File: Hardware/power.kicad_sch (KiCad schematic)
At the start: 57 parts, among them J8 DeployLipo, J9 UCLipo, Q10 DMP3099L, Q6 SI4143DY-T1-GE3, Q7 SI4143DY-T1-GE3, Q8 DMP3099L, Q9 DMP3099L, U10 LTC4412xS6, U11 MP28167GQ-A-Z, U14 LTC4412xS6, U16 SC4215, U17 LTC4412xS6, U22 LTC4412xS6, U9 LTC4412xS6

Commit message: black edition ordering stuff
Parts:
- added C37: 0.1uF, Capacitor_SMD:C_0402_1005Metric, symbol Device:C_Small
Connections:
- net GND: now also C37.1
- net UC_Lipo_Scaled: now also C37.2
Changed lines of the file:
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@@
   (junction (at 204.47 85.09) (diameter 0) (color 0 0 0 0)
   )
+  (junction (at 96.52 45.72) (diameter 0) (color 0 0 0 0)
+  )
   (junction (at 271.78 38.1) (diameter 0) (color 0 0 0 0)
   )
@@
   )
   (junction (at 38.1 160.02) (diameter 0) (color 0 0 0 0)
+  )
+  (junction (at 87.63 52.07) (diameter 0) (color 0 0 0 0)
   )
   (junction (at 207.01 90.17) (diameter 0) (color 0 0 0 0)
@@
   (no_connect (at 219.71 50.8))
   (no_connect (at 67.31 129.54))
-  (wire (pts (xy 87.63 45.72) (xy 100.33 45.72))
+  (wire (pts (xy 87.63 45.72) (xy 96.52 45.72))
     (stroke (width 0) (type default))
   )
@@
     (stroke (width 0) (type default))
   )
+  (wire (pts (xy 87.63 52.07) (xy 96.52 52.07))
+    (stroke (width 0) (type default))
+  )
   (wire (pts (xy 109.22 72.39) (xy 102.87 72.39))
     (stroke (width 0) (type default))
@@
     (stroke (width 0) (type default))
   )
+  (wire (pts (xy 96.52 46.99) (xy 96.52 45.72))
+    (stroke (width 0) (type default))
+  )
   (wire (pts (xy 271.78 83.82) (xy 281.94 83.82))
     (stroke (width 0) (type default))
@@
   )
   (wire (pts (xy 251.46 144.78) (xy 257.81 144.78))
+    (stroke (width 0) (type default))
+  )
+  (wire (pts (xy 96.52 45.72) (xy 100.33 45.72))
     (stroke (width 0) (type default))
   )
@@
         )
       )
+    )
+  )
+  (symbol (lib_id "Device:C_Small") (at 96.52 49.53 180) (unit 1)
+    (in_bom yes) (on_board yes) (dnp no)
+    (property "Reference" "C37" (at 99.4783 48.8354 0)
+      (effects (font (size 1.27 1.27)) (justify right) hide)
+    )
+    (property "Value" "0.1uF" (at 99.4783 51.3754 0)
+      (effects (font (size 1.27 1.27)) (justify right) hide)
+    )
+    (property "Footprint" "Capacitor_SMD:C_0402_1005Metric" (at 96.52 49.53 0)
+      (effects (font (size 1.27 1.27)) hide)
+    )
+    (property "Datasheet" "~" (at 96.52 49.53 0)
+      (effects (font (size 1.27 1.27)) hide)
+    )
+    (pin "1")
+    (pin "2")
+    (instances
+      (project "PickleRick"
+        (path "/e63e39d7-6ac0-4ffd-8aa3-1841a4541b55/150d7a0e-7d8c-4788-bc30-4a3682bf4d09"
+          (reference "C37") (unit 1)
+        )
+      )

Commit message: v3 hardware start
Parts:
- removed Q6, Q7: SI4143DY-T1-GE3, Package_SO:SOIC-8_3.9x4.9mm_P1.27mm, symbol Device:Q_PMOS_GDS
- added C58: 0.1uF, Capacitor_SMD:C_0402_1005Metric, symbol Device:C_Small
- added Q11, Q12: SQS141ELNW-T1_GE3, SQS850ENT1_GE3, symbol iclr-hw:SQS141ELNW-T1_GE3
- added R45: 80k, Resistor_SMD:R_0402_1005Metric, symbol Device:R_Small
- added R46: 10k, Resistor_SMD:R_0402_1005Metric, symbol Device:R_Small
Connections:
- net +24V: now also Q11.1 (S_1), Q11.2 (S_2), Q11.3 (S_3), Q12.1 (S_1), Q12.2 (S_2), Q12.3 (S_3), R45.1
- net Deploy_Lipo+: now also Q12.10 (D_6), Q12.11 (D_7), Q12.5 (D_1), Q12.6 (D_2), Q12.7 (D_3), Q12.8 (D_4), Q12.9 (D_5)
- net GND: now also C58.1, R46.2
- net RBUS_24V_IN: now also Q11.10 (D_6), Q11.11 (D_7), Q11.5 (D_1), Q11.6 (D_2), Q11.7 (D_3), Q11.8 (D_4), Q11.9 (D_5)
- net Deploy_Lipo_Gate: now reaches U14.5 (GATE)
- net Deploy_Lipo_Gate: now also Q12.4 (G)
- net RBUS_24V_GATE: now reaches U17.5 (GATE)
- net RBUS_24V_GATE: now also Q11.4 (G)
- net UC_Lipo_Scaled renamed Logic_Volt_Scaled
- new net Dep_Volt_Scaled: C58.2, R45.2, R46.1
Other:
- moved on the sheet: U14, U17

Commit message: more hardware updates
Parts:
- added 12VLED1: RED_LED, LED_SMD:LED_0402_1005Metric, symbol Device:LED_Small
- added C12: 4.7nF, Capacitor_SMD:C_0402_1005Metric, symbol Device:C_Small
- added C59: 10nF, Capacitor_SMD:C_0402_1005Metric, symbol Device:C_Small
- added IC1: TPS259830ONRGER, iclr-hw:TPS259830ONRGER, symbol iclr:TPS259830ONRGER
- added R10: 470, Resistor_SMD:R_0402_1005Metric, symbol Device:R_Small
- added R19: 1M, Capacitor_SMD:C_0402_1005Metric, symbol Device:R_Small
- added R20: 732k, Capacitor_SMD:C_0402_1005Metric, symbol Device:R_Small
- added R23: 73.2k, Capacitor_SMD:C_0402_1005Metric, symbol Device:R_Small
- added R24: 82, Capacitor_SMD:C_0402_1005Metric, symbol Device:R_Small
- added R47: 681, Capacitor_SMD:C_0402_1005Metric, symbol Device:R_Small
- Q11, Q12: footprint SQS850ENT1_GE3 -> iclr-hw:SQS850ENT1_GE3
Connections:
- net +24V: now also IC1.17 (OUT_1), IC1.18 (OUT_2), IC1.19 (OUT_3), IC1.20 (OUT_4), IC1.21 (OUT_5), IC1.22 (OUT_6), IC1.23 (OUT_7), IC1.24 (OUT_8); no longer Q11.1 (S_1), Q11.2 (S_2), Q11.3 (S_3), Q12.1 (S_1), Q12.2 (S_2), Q12.3 (S_3), R45.1, U14.6 (SENSE), U17.6 (SENSE)
- net Dep_Volt_Scaled: now also R10.1
- net GND: now also 12VLED1.1 (K), C12.1, C59.1, IC1.11 (NRETRY), IC1.14 (GND_3), IC1.26 (GND_4), IC1.4 (GND_1), IC1.5 (GND_2), R23.2, R24.2, R47.2
- new net: IC1.6 (EN/UVLO), R19.2, R20.1
- new net: C12.2, IC1.7 (ITIMER)
- new net: IC1.8 (ILIM), R24.1
- new net: 12VLED1.2 (A), R10.2
- new net DepCurrent: IC1.9 (IMON), R47.1
- new net EFUSE_IN: C59.2, IC1.1 (IN_1), IC1.16 (IN_4), IC1.2 (IN_2), IC1.25 (IN_5), IC1.3 (IN_3), Q11.1 (S_1), Q11.2 (S_2), Q11.3 (S_3), Q12.1 (S_1), Q12.2 (S_2), Q12.3 (S_3), R19.1, R45.1, U14.6 (SENSE), U17.6 (SENSE)
- new net OVLO: IC1.12 (OVLO), R20.2, R23.1
- no-connect marks 7 -> 10
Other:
- moved on the sheet: C29, C30, C31, C32, C33, C34, C35, C36, C38, C39, C40, C41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

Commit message: update
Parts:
- R47: value 681 -> 680
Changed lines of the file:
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@@
 			)
 		)
-		(property "Value" "681"
+		(property "Value" "680"
 			(at 122.9106 151.3261 0)
 			(effects

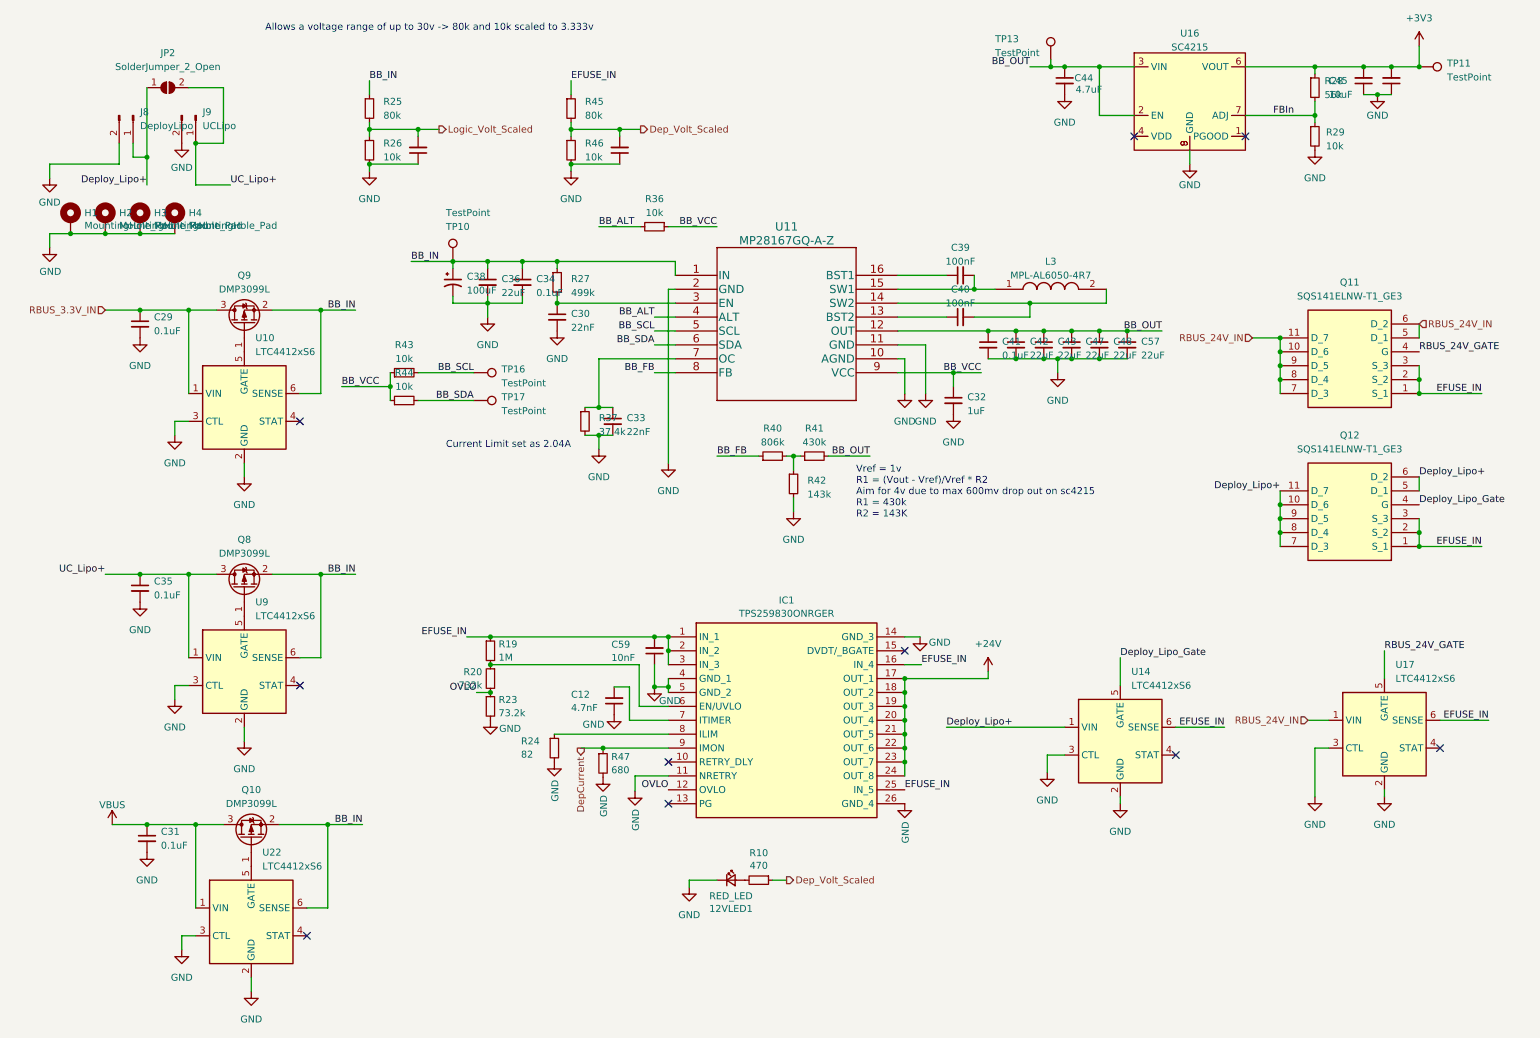
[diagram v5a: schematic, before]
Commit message: replaced efuse with ina219
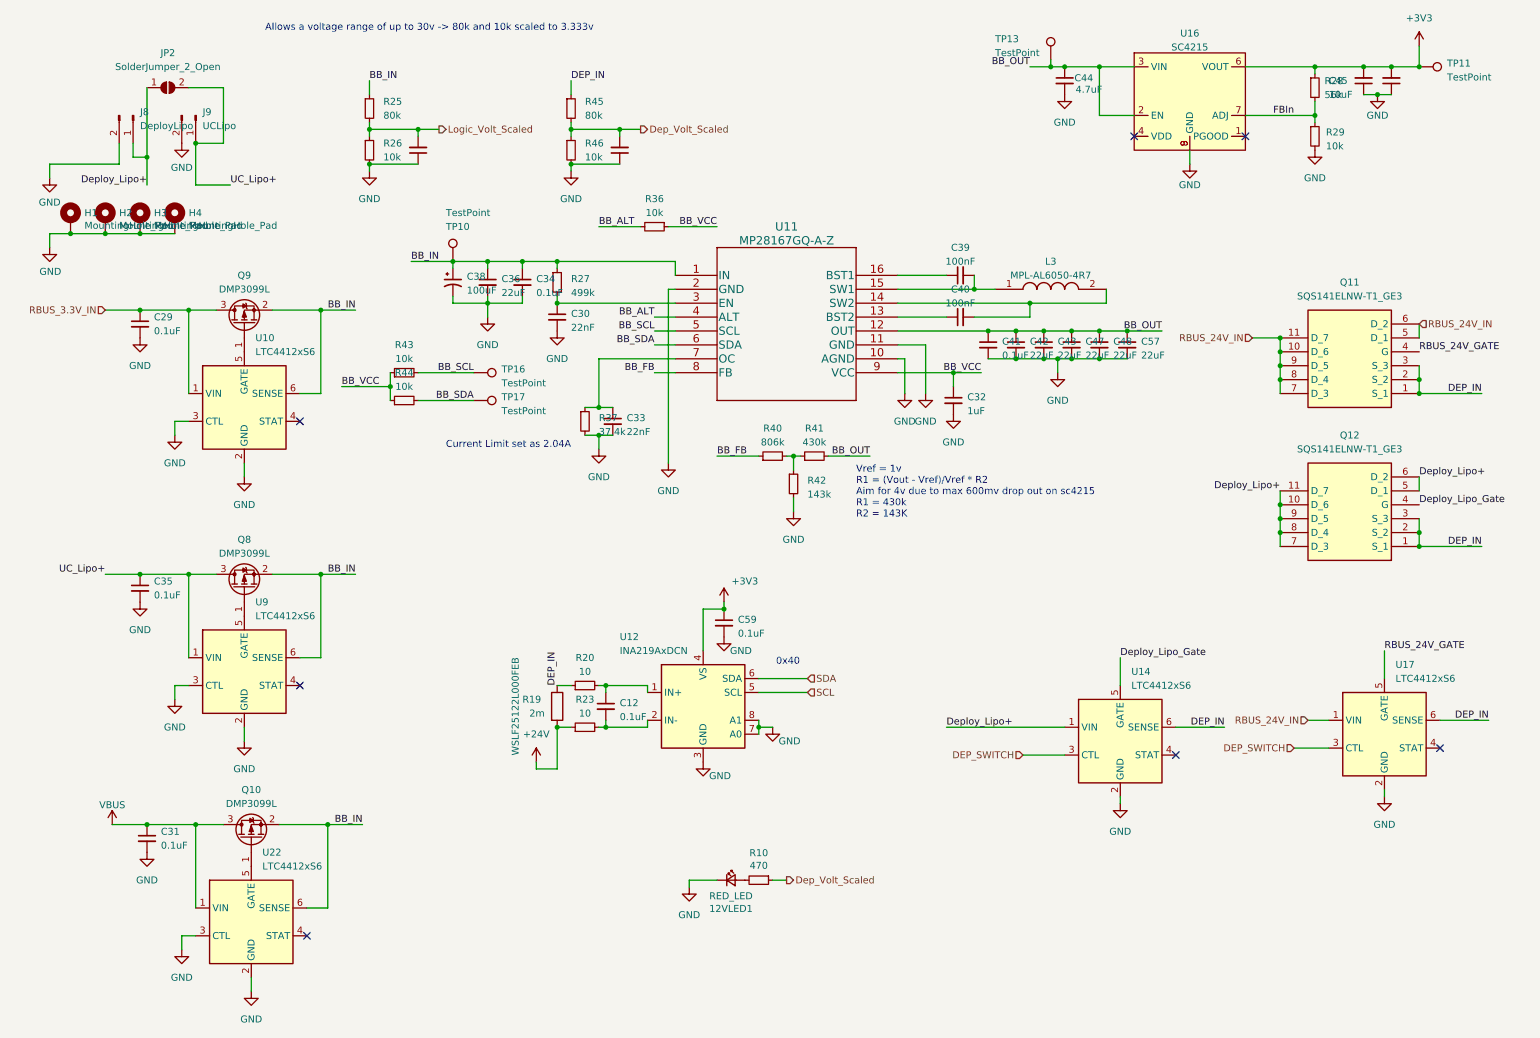
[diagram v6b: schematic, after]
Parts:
- removed IC1: TPS259830ONRGER, iclr-hw:TPS259830ONRGER, symbol iclr:TPS259830ONRGER
- removed R19: 1M, Capacitor_SMD:C_0402_1005Metric, symbol Device:R_Small
- removed R24: 82, Capacitor_SMD:C_0402_1005Metric, symbol Device:R_Small
- removed R47: 680, Capacitor_SMD:C_0402_1005Metric, symbol Device:R_Small
- added R19: 2m, Resistor_SMD:R_2512_6332Metric_Pad1.40x3.35mm_HandSolder, symbol Device:R
- added U12: INA219AxDCN, Package_TO_SOT_SMD:SOT-23-8, symbol Sensor_Energy:INA219AxDCN
- C12: value 4.7nF -> 0.1uF
- C59: value 10nF -> 0.1uF; MPN C1005X7S2A103KT000F -> (none)
- R20: value 732k -> 10; footprint Capacitor_SMD:C_0402_1005Metric -> Resistor_SMD:R_0402_1005Metric
- R23: value 73.2k -> 10; footprint Capacitor_SMD:C_0402_1005Metric -> Resistor_SMD:R_0402_1005Metric
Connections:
- net +24V: now also R23.1, R19.2
- net +3V3: now also C59.1, U12.4 (VS)
- net GND: now also C59.2, U12.3 (GND), U12.7 (A0), U12.8 (A1); no longer C12.1, C59.1, R23.2, U14.3 (CTL), U17.3 (CTL)
- net DEP_IN: now reaches R20.1
- net DEP_IN: now also Q11.1 (S_1), Q11.2 (S_2), Q11.3 (S_3), Q12.1 (S_1), Q12.2 (S_2), Q12.3 (S_3), R45.1, U14.6 (SENSE), U17.6 (SENSE), R19.1
- net at C12.2: now also R23.2, U12.2 (IN-)
- removed net EFUSE_IN: C59.2, Q11.1 (S_1), Q11.2 (S_2), Q11.3 (S_3), Q12.1 (S_1), Q12.2 (S_2), Q12.3 (S_3), R45.1, U14.6 (SENSE), U17.6 (SENSE)
- net OVLO: no longer names the net of R20.2
- net OVLO: now also C12.1, U12.1 (IN+); no longer R23.1
- new net DEP_SWITCH: U14.3 (CTL), U17.3 (CTL)
- new net SCL: U12.5 (SCL)
- new net SDA: U12.6 (SDA)
- no-connect marks 10 -> 7
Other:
- note added: "0x40"

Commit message: fixes
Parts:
- added IC1: MIC5060YML-TR, SON65P300X300X100-9N-D, symbol iclr-hw:MIC5060YML-TR
- added Q5: BSZ025N04LS, iclr-hw:BSZ025N04LS, symbol iclr-hw:BSZ025N04LS
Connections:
- net +24V: now also IC1.3 (SOURCE), Q5.1 (S), Q5.2 (S), Q5.3 (S), Q5.A1 (S); no longer R19.2, R23.1
- net DEP_SWITCH: now also IC1.2 (INPUT); no longer U14.3 (CTL), U17.3 (CTL)
- net GND: now also IC1.4 (GND), IC1.9 (EP)
- new net: IC1.5 (GATE), Q5.4 (G)
- new net DEP_SWITCH_IN: IC1.1 (V+), Q5.5 (D), Q5.6 (D), Q5.7 (D), Q5.8 (D), Q5.A5 (D), R19.2, R23.1
- no-connect marks 7 -> 12
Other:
- moved on the sheet: 12VLED1, C12, C59, R10, R19, R20, R23, U12

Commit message: update
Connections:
- net +3V3: now also U12.7 (A0), U12.8 (A1)
- net GND: no longer U12.7 (A0), U12.8 (A1)
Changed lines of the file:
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@@
+	)
+	(symbol
+		(lib_id "power:+3V3")
+		(at 134.62 128.27 0)
+		(unit 1)
+		(exclude_from_sim no)
+		(in_bom yes)
+		(on_board yes)
+		(dnp no)
+		(fields_autoplaced yes)
+		(property "Reference" "#PWR0113"
+			(at 134.62 132.08 0)
+			(effects
+				(font
+					(size 1.27 1.27)
+				)
+				(hide yes)
+			)
+		)
+		(property "Value" "+3V3"
+			(at 134.62 123.19 0)
+			(effects
+				(font
+					(size 1.27 1.27)
+				)
+			)
+		)
+		(property "Footprint" ""
+			(at 134.62 128.27 0)
+			(effects
+				(font
+					(size 1.27 1.27)
+				)
+				(hide yes)
+			)
+		)
+		(property "Datasheet" ""
+			(at 134.62 128.27 0)
+			(effects
+				(font
+					(size 1.27 1.27)
+				)
+				(hide yes)
+			)
+		)
+		(property "Description" "Power symbol creates a global label with name \"+3V3\""
+			(at 134.62 128.27 0)
+			(effects
+				(font
+					(size 1.27 1.27)
+				)
+				(hide yes)
+			)
+		)
+		(pin "1"
+		)
+		(instances
+			(project ""
+				(path "/e63e39d7-6ac0-4ffd-8aa3-1841a4541b55/150d7a0e-7d8c-4788-bc30-4a3682bf4d09"
+					(reference "#PWR0113")
+					(unit 1)
+				)
+			)
+		)
 	)
 	(symbol
@@
 					(unit 1)
 				)
-			)
-		)
-	)
-	(symbol
-		(lib_id "power:GND")
-		(at 134.62 128.27 0)
-		(unit 1)
-		(exclude_from_sim no)
-		(in_bom yes)
-		(on_board yes)
-		(dnp no)
-		(property "Reference" "#PWR0113"
-			(at 134.62 134.62 0)
-			(effects
-				(font
-					(size 1.27 1.27)
-				)
-				(hide yes)
-			)
-		)
-		(property "Value" "GND"
-			(at 139.7 130.81 0)
-			(effects
-				(font
-					(size 1.27 1.27)
-				)
-				(justify right)
-			)
-		)
-		(property "Footprint" ""
-			(at 134.62 128.27 0)
-			(effects
-				(font
-					(size 1.27 1.27)
-				)
-				(hide yes)
-			)
-		)
-		(property "Datasheet" ""
-			(at 134.62 128.27 0)
-			(effects
-				(font
-					(size 1.27 1.27)
-				)
-				(hide yes)
-			)
-		)
-		(property "Description" ""
-			(at 134.62 128.27 0)
-			(effects
-				(font
-					(size 1.27 1.27)
-				)
-				(hide yes)
-			)
-		)
-		(pin "1"
-		)
-		(instances
-			(project "PickleRick"
-				(path "/e63e39d7-6ac0-4ffd-8aa3-1841a4541b55/150d7a0e-7d8c-4788-bc30-4a3682bf4d09"
-					(reference "#PWR0113")
-					(unit 1)
-				)
